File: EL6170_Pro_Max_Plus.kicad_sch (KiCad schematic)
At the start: 229 parts, among them CN1 PJ-327A0-SMT, J1 USB_C_Receptacle, J2 microSD, Q1 MMBT3904, Q2 MMBT3904, Q3 2N7002, Q4 AO3401A, Q5 AO3401A, SW1 SW_LEFT, SW10 SW_K4, SW11 SW_K5, SW12 SW_K6, SW13 SW_K7, SW14 SW_K8, SW15 SW_K9, SW16 SW_K0, SW17 SW_KQ, SW18 SW_KW, SW19 SW_KE, SW2 SW_UP, SW20 SW_KR, SW21 SW_KT, SW22 SW_KY, SW23 SW_KU, SW24 SW_KI, SW25 SW_KO, SW26 SW_KP, SW27 SW_KA, SW28 SW_KS, SW29 SW_KD, SW3 SW_DOWN, SW30 SW_KF, SW31 SW_KG, SW32 SW_KH, SW33 SW_KJ, SW34 SW_KK, SW35 SW_KL, SW36 SW_KZ, SW37 SW_KX, SW38 SW_KC, SW39 SW_KV, SW4 SW_RIGHT, SW40 SW_KB, SW41 SW_KN, SW42 SW_KM, SW43 SW_KCOM, SW44 SW_KDOT, SW45 SW_SHIFT, SW46 SW_CE(IO0), SW47 SW_OFF, SW48 SW_SECRET, SW49 SW_MCK, SW5 SW_UP2, SW50 SW_SPACE, SW51 SW_REMARK, SW52 SW_CALENDAR, SW53 SW_MODE, SW54 SW_ENTER, SW6 SW_DOWN2, SW7 SW_K1, SW8 SW_K2, SW9 SW_K3, U1 ESP32-S3, U10 ME6211C33M5, U11 TP5400_C2891434, U12 PCF8575DBR, U2 TPS61040DBV, U3 ESP-PSRAM64H, U4 W25Q128JVS, U5 ME6217C33M5, U6 CH340K, U7 RFANT5220110A0T, U8 CH334R, U9 PCM5102A, X1 40MHz, X2 12MHz

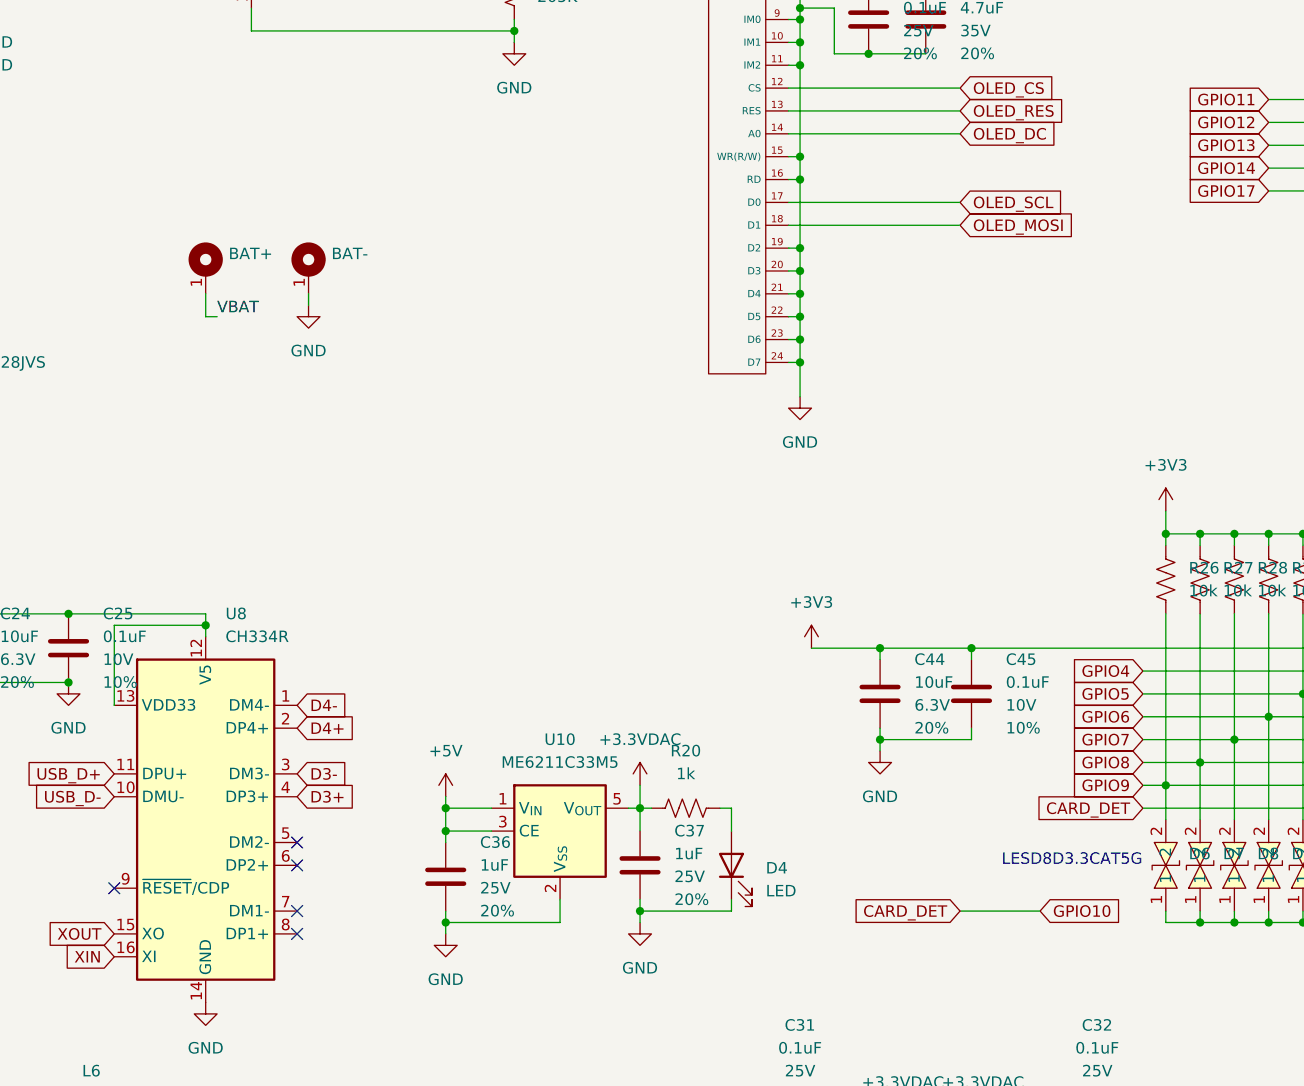
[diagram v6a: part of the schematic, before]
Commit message: add some keypad
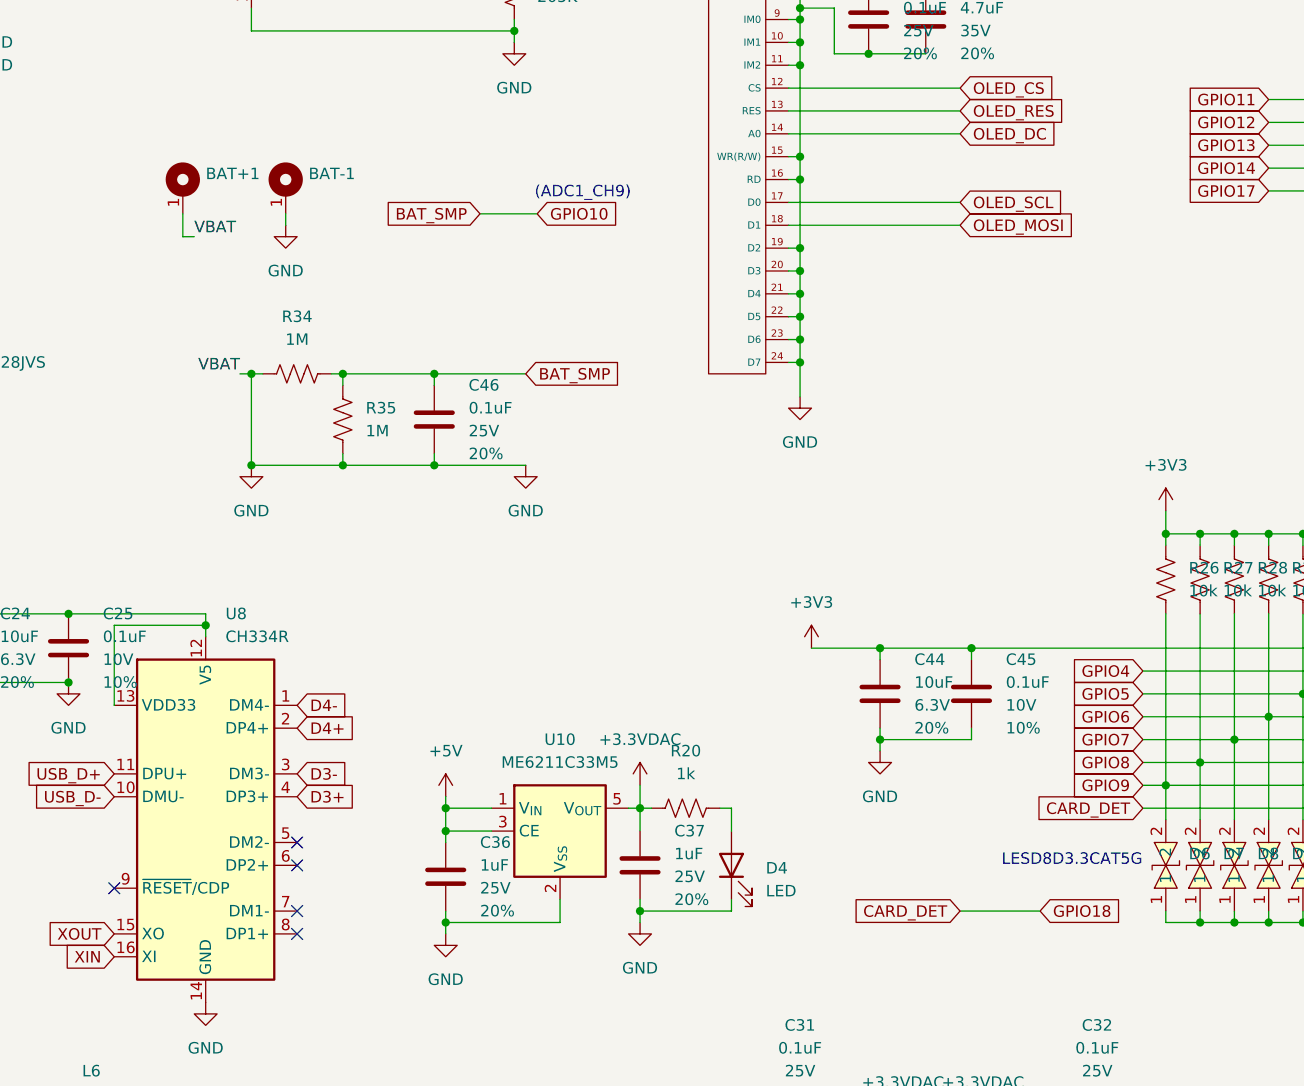
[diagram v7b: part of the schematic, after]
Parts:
- added C46: 0.1uF, SparkFun-Capacitor:C_0603_1608Metric, symbol SparkFun-Capacitor:0.1uF_0603_25V_20%
- added R34, R35: 1M, SparkFun-Resistor:R_0603_1608Metric, symbol SparkFun-Resistor:1M_0603
- renumbered BAT+ to BAT+1, BAT- to BAT-1
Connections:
- net GPIO18 is gone; now on net CARD_DET: U1.24 (GPIO18)
- net VBAT is gone; now on net GND: BAT+1.1, C40.1, C41.1, C42.1, L6.2, U11.6 (BAT)
- net CARD_DET: no longer U1.15 (GPIO10)
- net GND: now also C46.2, R34.2, R35.2
- new net BAT_SMP: C46.1, R34.1, R35.1, U1.15 (GPIO10)
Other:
- note added: "(ADC1_CH9)"
- moved on the sheet: BAT+1, BAT-1

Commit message: sync
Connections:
- net GND: no longer BAT+1.1, C40.1, C41.1, C42.1, L6.2, R34.2, U11.6 (BAT)
- new net VBAT: BAT+1.1, C40.1, C41.1, C42.1, L6.2, R34.2, U11.6 (BAT)
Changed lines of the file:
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@@
 	)
 	(junction
-		(at 256.54 95.25)
-		(diameter 0)
-		(color 0 0 0 0)
-	)
-	(junction
 		(at 251.46 113.03)
 		(diameter 0)
@@
 	)
 	(junction
-		(at 256.54 85.09)
-		(diameter 0)
-		(color 0 0 0 0)
-	)
-	(junction
 		(at 142.24 264.16)
 		(diameter 0)
@@
 	(wire
 		(pts
-			(xy 256.54 85.09) (xy 257.81 85.09)
-		)
-		(stroke
-			(width 0)
-			(type default)
-		)
-	)
-	(wire
-		(pts
 			(xy 124.46 68.58) (xy 110.49 68.58)
 		)
@@
 	(wire
 		(pts
-			(xy 256.54 85.09) (xy 256.54 95.25)
-		)
-		(stroke
-			(width 0)
-			(type default)
-		)
-	)
-	(wire
-		(pts
 			(xy 227.33 189.23) (xy 254 189.23)
 		)
@@
 	(wire
 		(pts
-			(xy 255.27 85.09) (xy 256.54 85.09)
+			(xy 255.27 85.09) (xy 257.81 85.09)
 		)
 		(stroke
